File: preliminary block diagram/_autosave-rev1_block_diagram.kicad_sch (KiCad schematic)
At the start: 16 parts, among them SW1 ???, U29 LMX2594+100MHz oscillator, U30 PA, U31 HMC451, U32 LNA, U33 ADP-2-1W, U34 10dB, U35 Mixer, U37 Mixer, U39 ADP-2-1W

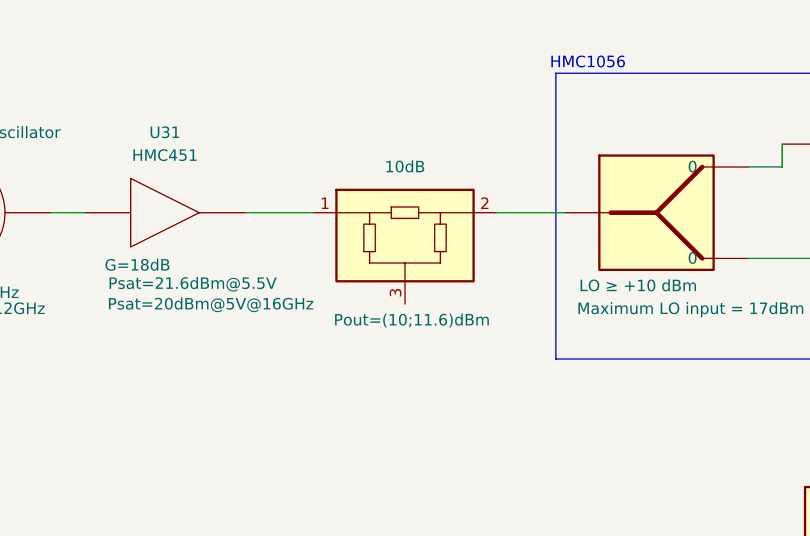
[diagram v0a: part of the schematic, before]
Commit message: added description to the block diagram
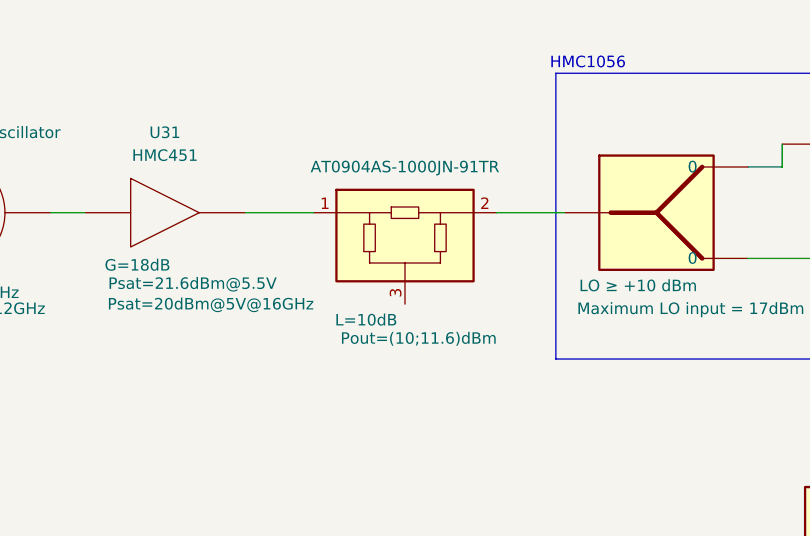
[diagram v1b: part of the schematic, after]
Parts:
- U34: value 10dB -> AT0904AS-1000JN-91TR; footprint RF_Converter:RF_Attenuator_Susumu_PAT1220 -> (none); Field6 (none) -> L=10dB
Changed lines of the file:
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@@
 			)
 		)
-		(property "Value" "10dB"
+		(property "Value" "AT0904AS-1000JN-91TR"
 			(at 86.36 85.09 0)
 			(effects
@@
 			)
 		)
-		(property "Footprint" "RF_Converter:RF_Attenuator_Susumu_PAT1220"
+		(property "Footprint" ""
 			(at 86.36 92.71 0)
 			(effects
@@
 			)
 		)
-		(property "Datasheet" "https://www.susumu.co.jp/common/pdf/n_catalog_partition16_en.pdf"
+		(property "Datasheet" "https://cz.mouser.com/en/ProductDetail/Vishay-Barry-Industries/AT0904AS-1000JN-91TR?qs=ulEaXIWI0c9CMXIQQzzR1g%3D%3D"
 			(at 80.01 86.36 0)
 			(effects
@@
 		)
 		(property "Description" "Pout=(10;11.6)dBm"
-			(at 87.122 102.108 0)
+			(at 87.884 104.14 0)
 			(effects
 				(font
+					(size 1.27 1.27)
+				)
+			)
+		)
+		(property "Field5" ""
+			(at 86.36 92.71 0)
+			(effects
+				(font
+					(size 1.27 1.27)
+				)
+				(hide yes)
+			)
+		)
+		(property "Field6" "L=10dB"
+			(at 82.042 102.108 0)
+			(effects
+				(font
